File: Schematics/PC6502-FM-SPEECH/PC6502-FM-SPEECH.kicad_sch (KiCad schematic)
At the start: 20 parts, among them J1 BUS, J5 Conn_02x05_Odd_Even, U1 ATF1502AS, X2 CXO_DIP8

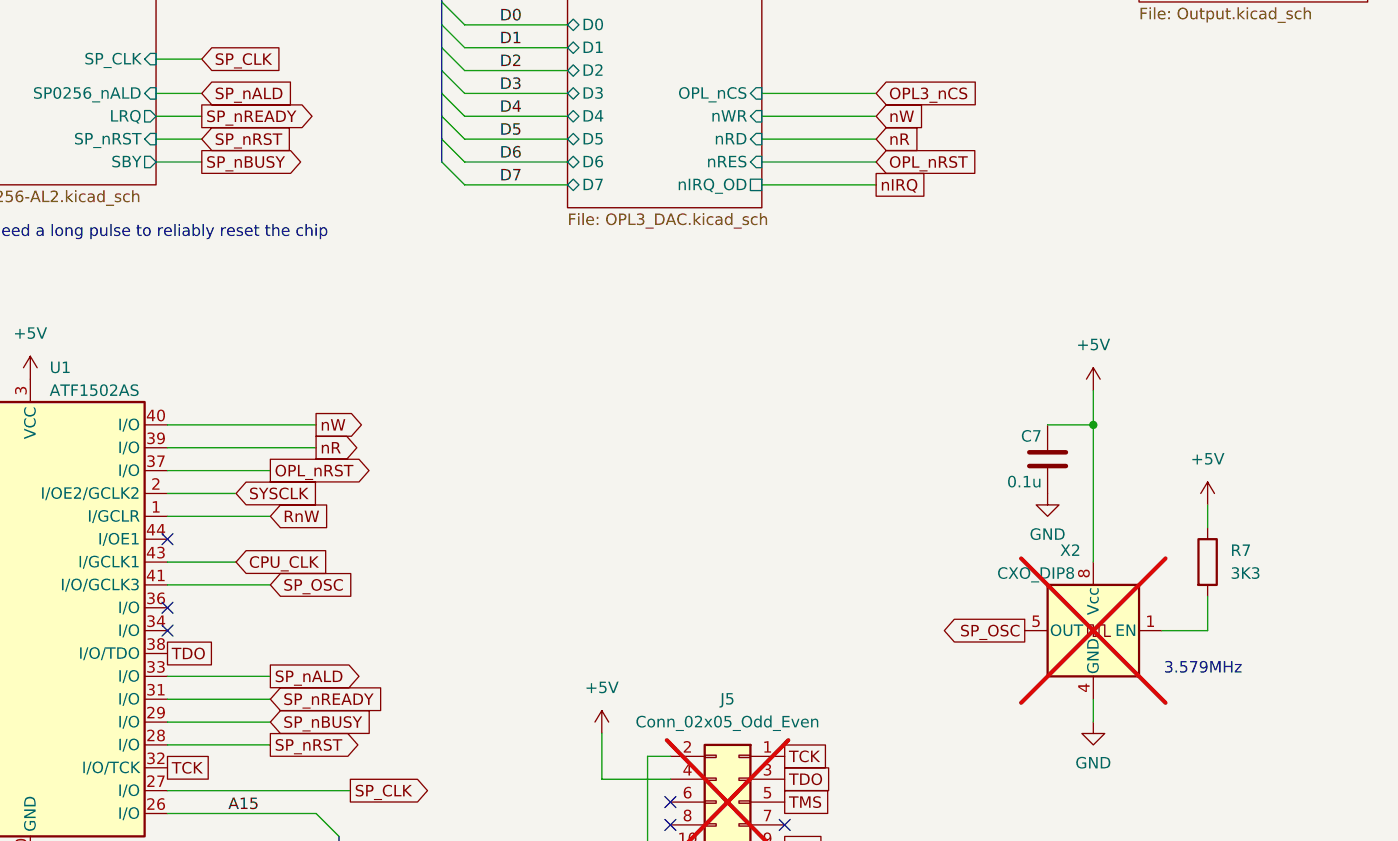
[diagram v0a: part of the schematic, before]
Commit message: CPU CPLD UPDATE!!
CPU will now run at 14MHz with the updated code in the CPLD
Begun assembly of Speech/FM board
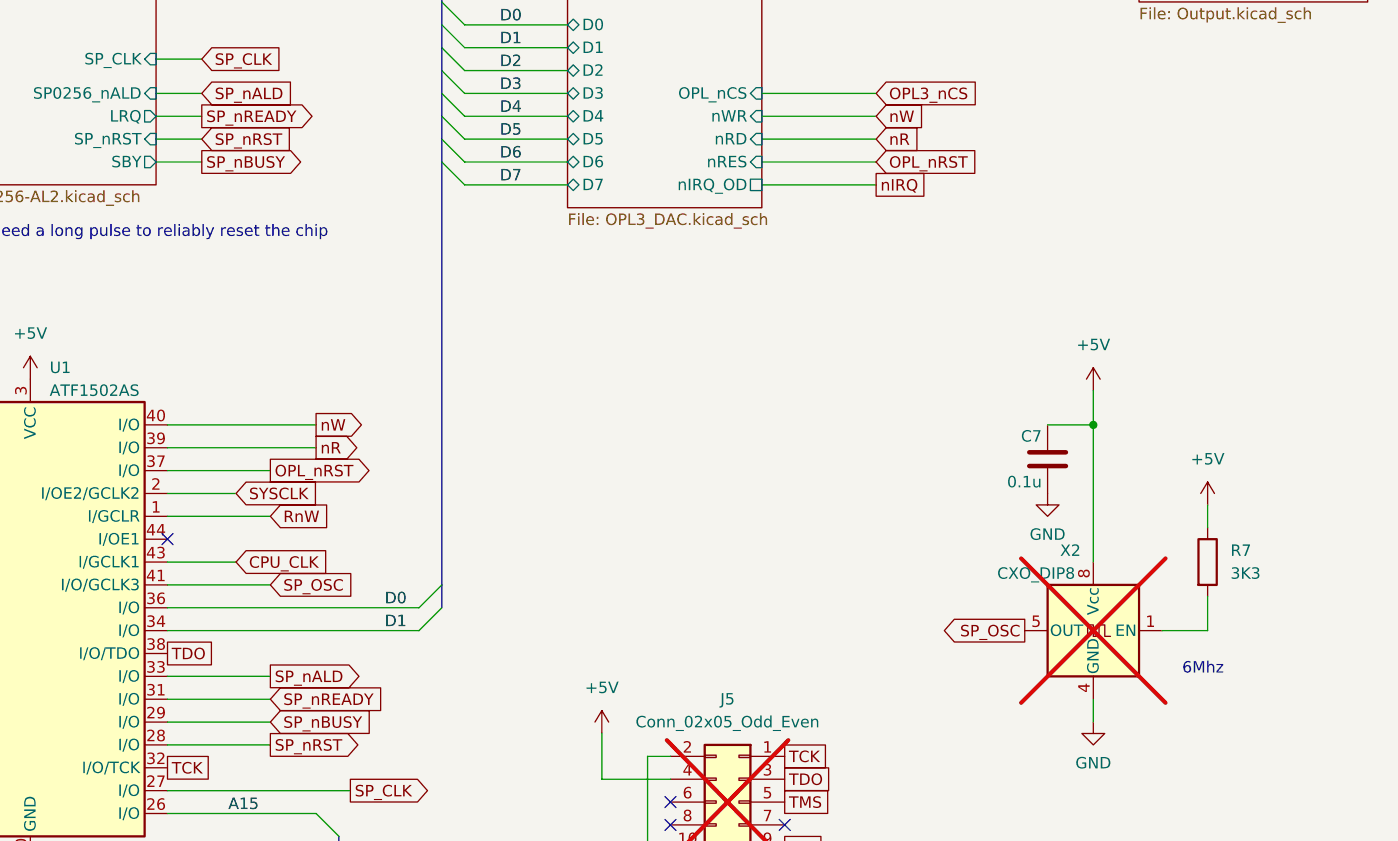
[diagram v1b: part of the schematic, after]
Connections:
- net D0: now also U1.36 (I/O)
- net D1: now also U1.34 (I/O)
- no-connect marks 8 -> 6
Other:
- note added: "6Mhz"
- note removed: "3.579MHz"
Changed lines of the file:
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@@
 		)
 	)
-	(text "3.579MHz\n"
+	(text "6Mhz\n"
 		(exclude_from_sim no)
 		(at 256.032 119.888 0)
@@
 	)
 	(no_connect
-		(at 140.97 115.57)
-	)
-	(no_connect
 		(at 196.85 134.62)
 	)
@@
 		(at 38.1 106.68)
 	)
-	(no_connect
-		(at 140.97 113.03)
-	)
 	(bus_entry
 		(at 71.12 86.36)
@@
 	)
 	(bus_entry
+		(at 168.91 113.03)
+		(size 2.54 -2.54)
+		(stroke
+			(width 0)
+			(type default)
+		)
+	)
+	(bus_entry
 		(at 173.99 66.04)
 		(size -2.54 -2.54)
@@
 	)
 	(bus_entry
+		(at 168.91 115.57)
+		(size 2.54 -2.54)
+		(stroke
+			(width 0)
+			(type default)
+		)
+	)
+	(bus_entry
 		(at 71.12 60.96)
 		(size 2.54 -2.54)
@@
 	(wire
 		(pts
+			(xy 140.97 113.03) (xy 168.91 113.03)
+		)
+		(stroke
+			(width 0)
+			(type default)
+		)
+	)
+	(wire
+		(pts
 			(xy 36.83 53.34) (xy 36.83 48.26)
 		)
@@
 		)
 	)
+	(bus
+		(pts
+			(xy 171.45 110.49) (xy 171.45 113.03)
+		)
+		(stroke
+			(width 0)
+			(type default)
+		)
+	)
 	(wire
 		(pts
@@
 	(wire
 		(pts
+			(xy 140.97 115.57) (xy 168.91 115.57)
+		)
+		(stroke
+			(width 0)
+			(type default)
+		)
+	)
+	(wire
+		(pts
 			(xy 38.1 43.18) (xy 36.83 43.18)
 		)
@@
 		(pts
 			(xy 93.98 135.89) (xy 110.49 135.89)
+		)
+		(stroke
+			(width 0)
+			(type default)
+		)
+	)
+	(bus
+		(pts
+			(xy 171.45 63.5) (xy 171.45 110.49)
 		)
 		(stroke
@@
 		)
 	)
+	(label "D0"
+		(at 165.1 113.03 0)
+		(effects
+			(font
+				(size 1.27 1.27)
+			)
+			(justify left bottom)
+		)
+	)
 	(label "A6"
 		(at 99.06 115.57 180)
@@
 		(effects
 			(font
+				(size 1.27 1.27)
+			)
+			(justify left bottom)
+		)
+	)
+	(label "D1"
+		(at 165.1 115.57 0)
+		(effects
+			(font

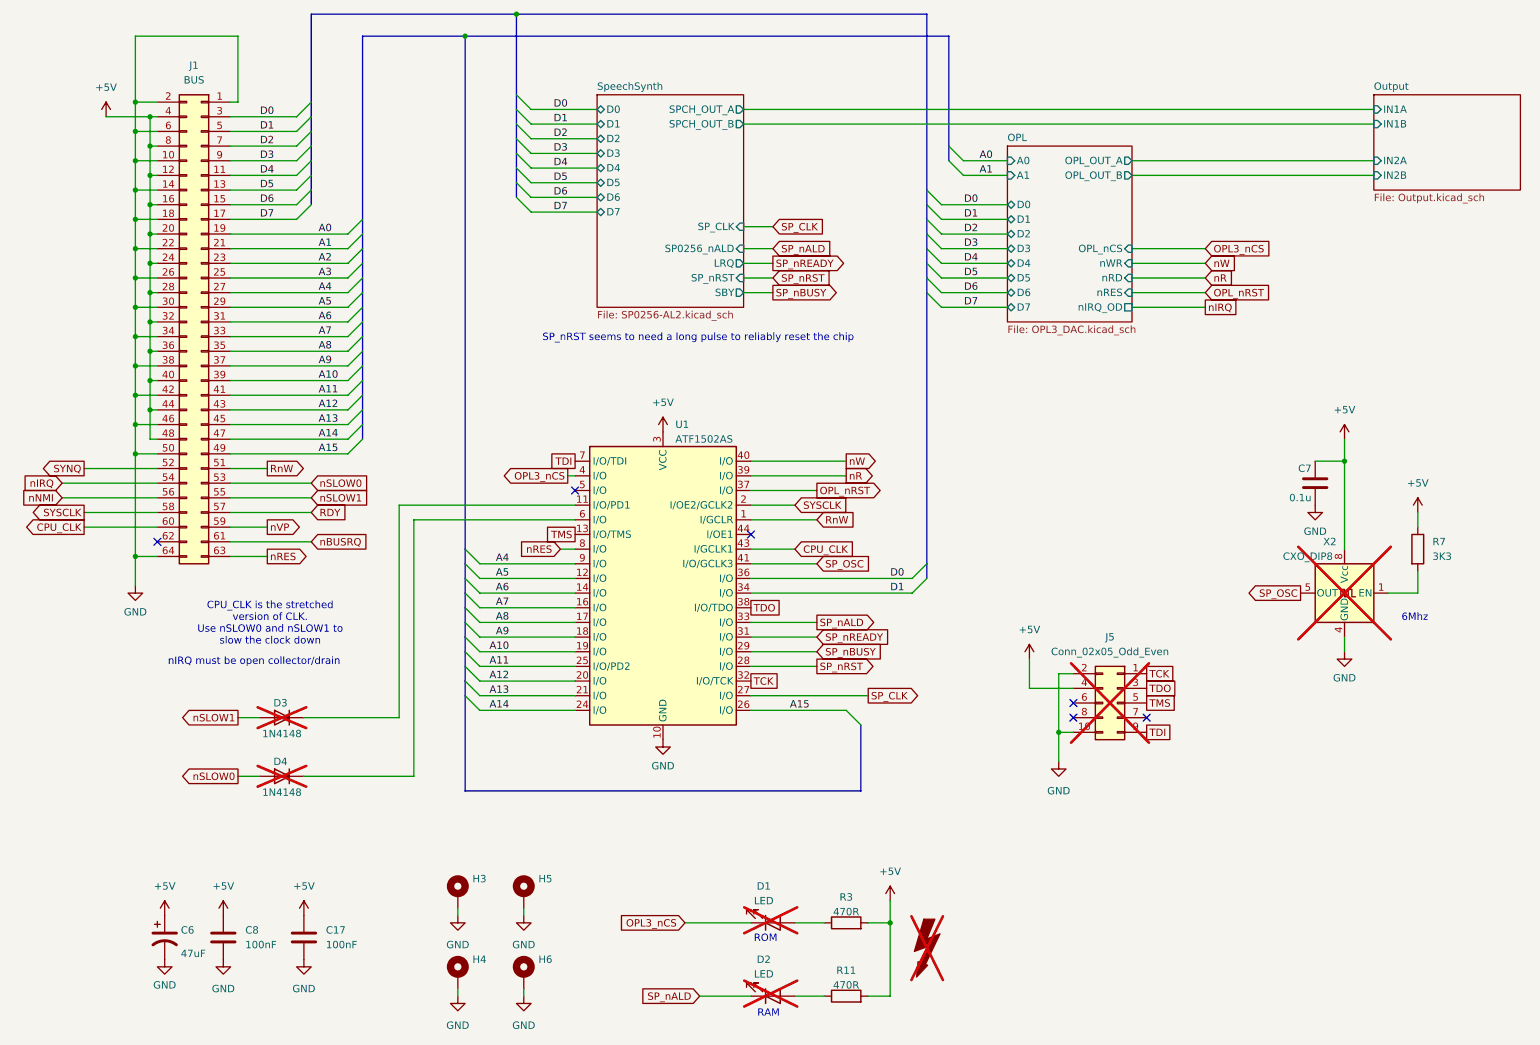
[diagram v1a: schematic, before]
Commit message: SP0256 Speech synth working
SP0256 now working, couple of extra wires needed, but PCB and schematics updated.
Test code (SP0256_TEST3.BAS) created.
CPLD updated.
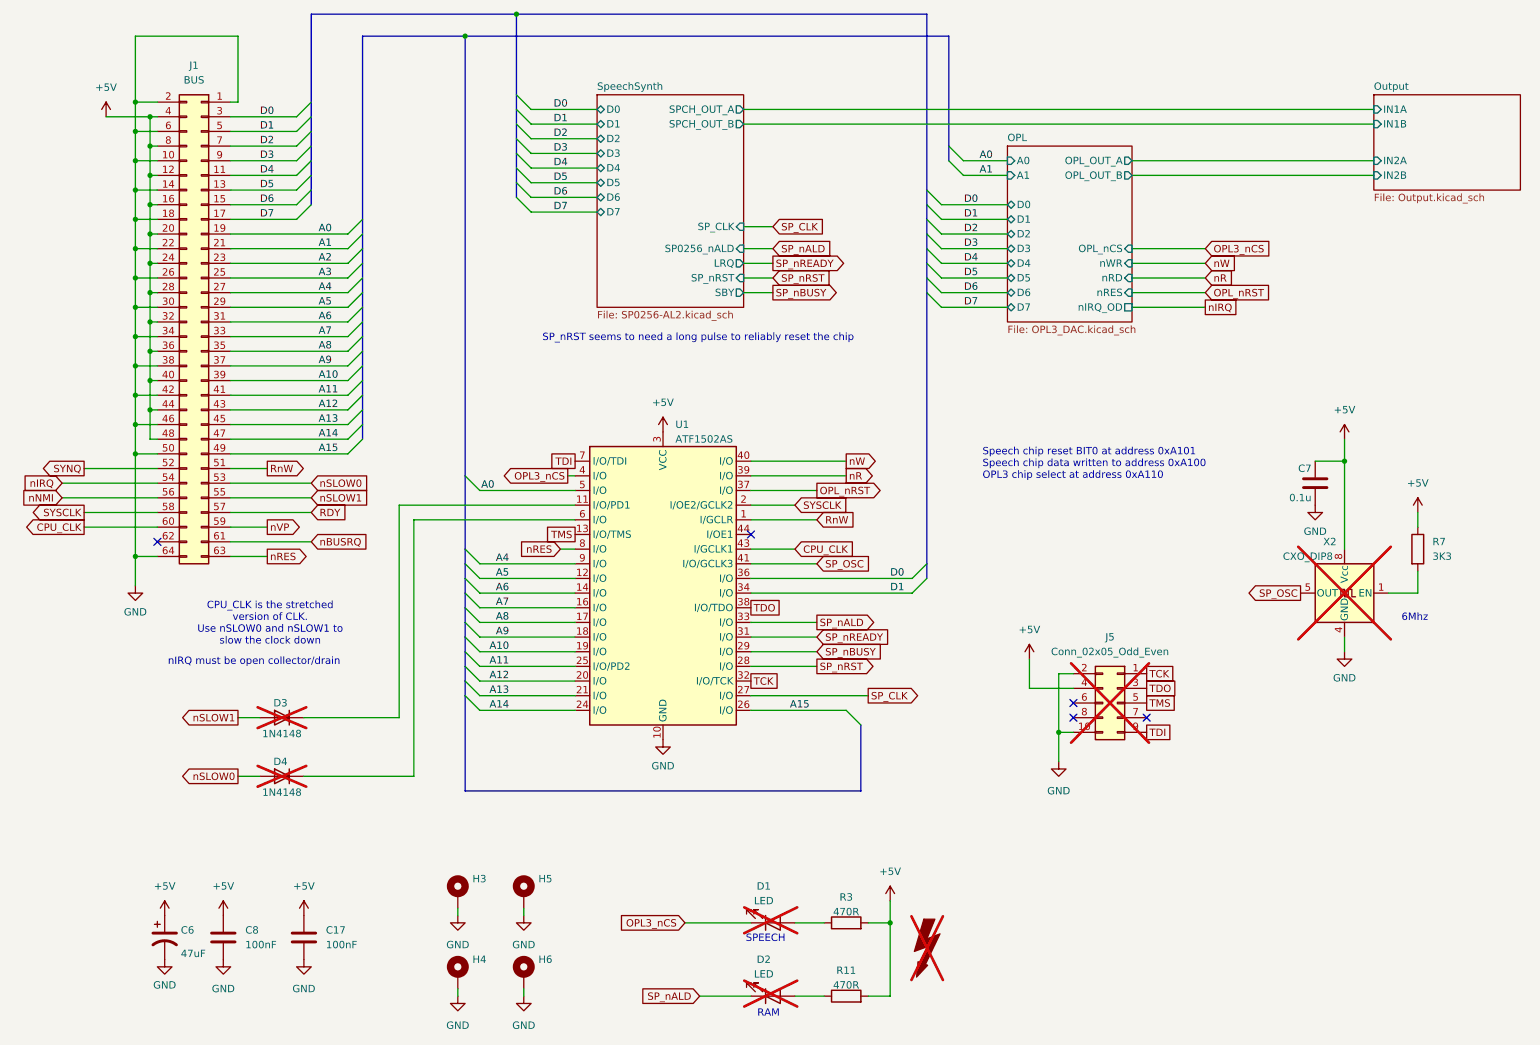
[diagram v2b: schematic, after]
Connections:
- net A0: now also U1.5 (I/O)
- no-connect marks 6 -> 5
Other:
- note added: "SPEECH"
- note added: "Speech chip reset BIT0 at address 0xA101 Speech chip data written to address 0xA100 OPL3 chip select at address 0xA110"
- note removed: "ROM"
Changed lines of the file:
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@@
 		)
 	)
+	(text "Speech chip reset BIT0 at address 0xA101\nSpeech chip data written to address 0xA100\nOPL3 chip select at address 0xA110"
+		(exclude_from_sim no)
+		(at 181.102 93.218 0)
+		(effects
+			(font
+				(size 1.27 1.27)
+			)
+			(justify left)
+		)
+	)
 	(text "SP_nRST seems to need a long pulse to reliably reset the chip"
 		(exclude_from_sim no)
@@
 		)
 	)
-	(text "ROM"
+	(text "SPEECH\n"
 		(exclude_from_sim no)
 		(at 143.51 175.514 0)
@@
 	)
 	(no_connect
-		(at 110.49 97.79)
-	)
-	(no_connect
 		(at 140.97 105.41)
 	)
@@
 	)
 	(bus_entry
+		(at 93.98 97.79)
+		(size -2.54 -2.54)
+		(stroke
+			(width 0)
+			(type default)
+		)
+	)
+	(bus_entry
 		(at 93.98 120.65)
 		(size -2.54 -2.54)
@@
 	(wire
 		(pts
+			(xy 93.98 97.79) (xy 110.49 97.79)
+		)
+		(stroke
+			(width 0)
+			(type default)
+		)
+	)
+	(wire
+		(pts
 			(xy 64.77 99.06) (xy 50.8 99.06)
 		)
@@
 		)
 	)
+	(bus
+		(pts
+			(xy 91.44 95.25) (xy 91.44 107.95)
+		)
+		(stroke
+			(width 0)
+			(type default)
+		)
+	)
 	(wire
 		(pts
@@
 	(bus
 		(pts
-			(xy 91.44 19.05) (xy 91.44 107.95)
+			(xy 91.44 19.05) (xy 91.44 95.25)
 		)
 		(stroke
@@
 		(effects
 			(font
+				(size 1.27 1.27)
+			)
+			(justify right bottom)
+		)
+	)
+	(label "A0"
+		(at 96.52 97.79 180)
+		(effects
+			(font

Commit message: Updated Schematics and CPLD files
Files updated for the CPU & FM Speech board
Also revised CPLDs for CPU, VIA and Compact Flasg
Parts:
- D3, D4, J5, X2: now fitted
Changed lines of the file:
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@@
 		(in_bom yes)
 		(on_board yes)
-		(dnp yes)
+		(dnp no)
 		(property "Reference" "D3"
 			(at 59.436 134.62 0)
@@
 		(in_bom yes)
 		(on_board yes)
-		(dnp yes)
+		(dnp no)
 		(fields_autoplaced yes)
 		(property "Reference" "J5"
@@
 		(in_bom yes)
 		(on_board yes)
-		(dnp yes)
+		(dnp no)
 		(property "Reference" "D4"
 			(at 59.436 144.78 0)
@@
 		(in_bom yes)
 		(on_board yes)
-		(dnp yes)
+		(dnp no)
 		(property "Reference" "X2"
 			(at 241.3 106.68 0)

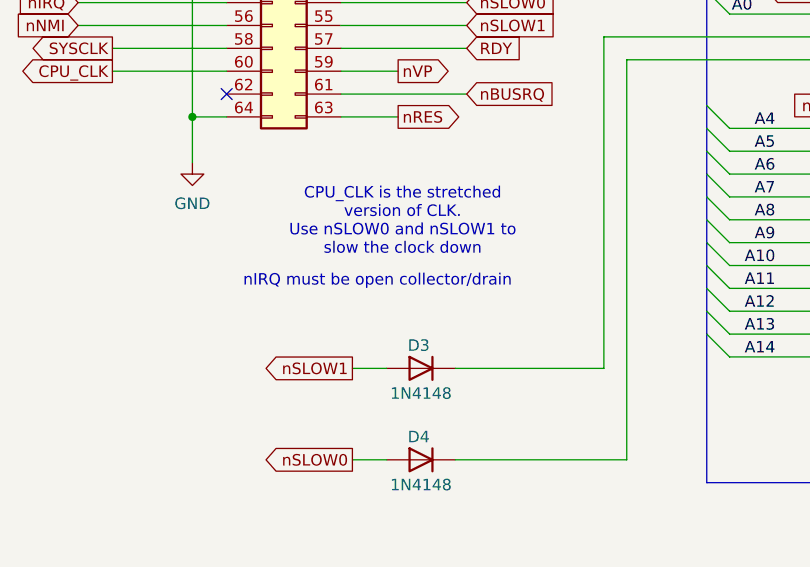
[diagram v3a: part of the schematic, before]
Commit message: Found an issue with Sound/Speech PCB, resolved
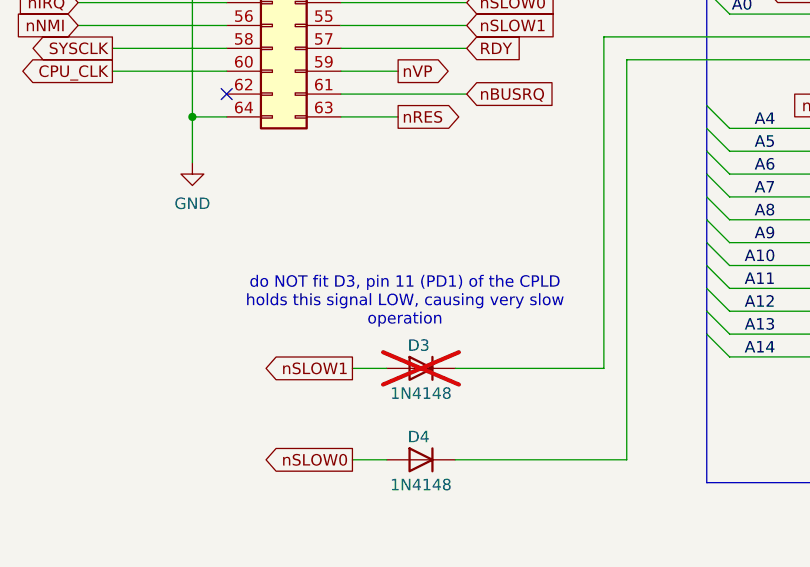
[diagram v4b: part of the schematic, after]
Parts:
- D3: now not fitted
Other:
- note added: "do NOT fit D3, pin 11 (PD1) of the CPLD holds this signal LOW, causing very slow operation"
- note removed: "CPU_CLK is the stretched version of CLK. Use nSLOW0 and nSLOW1 to slow the clock down"
- note removed: "nIRQ must be open collector/drain"
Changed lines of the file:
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@@
 		)
 	)
-	(text "CPU_CLK is the stretched\nversion of CLK. \nUse nSLOW0 and nSLOW1 to\nslow the clock down"
+	(text "do NOT fit D3, pin 11 (PD1) of the CPLD\nholds this signal LOW, causing very slow\noperation"
 		(exclude_from_sim no)
-		(at 57.658 120.904 0)
+		(at 57.912 129.794 0)
 		(effects
 			(font
@@
 		)
 	)
-	(text "nIRQ must be open collector/drain"
-		(exclude_from_sim no)
-		(at 54.864 127.508 0)
-		(effects
-			(font
-				(size 1.27 1.27)
-			)
-		)
-	)
 	(junction
 		(at 36.83 43.18)
@@
 		(in_bom yes)
 		(on_board yes)
-		(dnp no)
+		(dnp yes)
 		(property "Reference" "D3"
 			(at 59.436 134.62 0)
